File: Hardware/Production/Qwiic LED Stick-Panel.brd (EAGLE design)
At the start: 111.5 x 169.2 mm, 558 parts, among them J13 QWIIC_RA, J14 QWIIC_RA, J15 AVR_SPI_PROG_3X2TESTPOINTS, J19 QWIIC_RA, J2 QWIIC_RA, J20 QWIIC_RA, J21 AVR_SPI_PROG_3X2TESTPOINTS, J25 QWIIC_RA, J26 QWIIC_RA, J27 AVR_SPI_PROG_3X2TESTPOINTS, J3 QWIIC_RA, J31 QWIIC_RA, J32 QWIIC_RA, J33 AVR_SPI_PROG_3X2TESTPOINTS, J4 QWIIC_RA, J6 AVR_SPI_PROG_3X2TESTPOINTS, J8 QWIIC_RA, J9 AVR_SPI_PROG_3X2TESTPOINTS, U1 ATTINY85, U2 ATTINY85, U3 ATTINY85, U4 ATTINY85, U5 ATTINY85, U6 ATTINY85

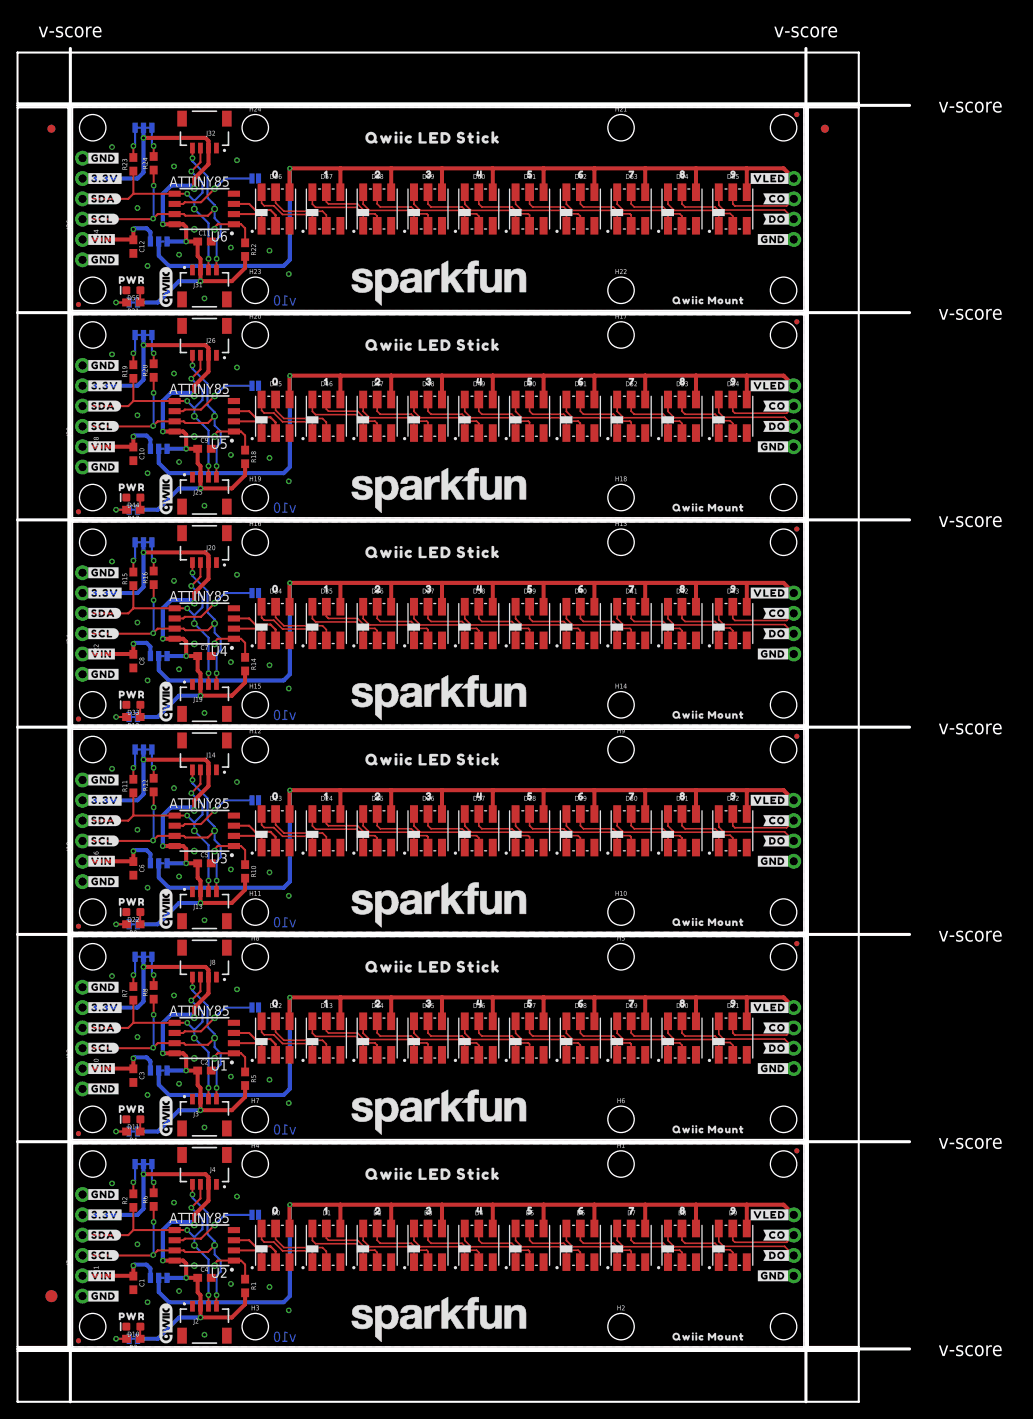
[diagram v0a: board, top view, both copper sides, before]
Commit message: Re-panelize
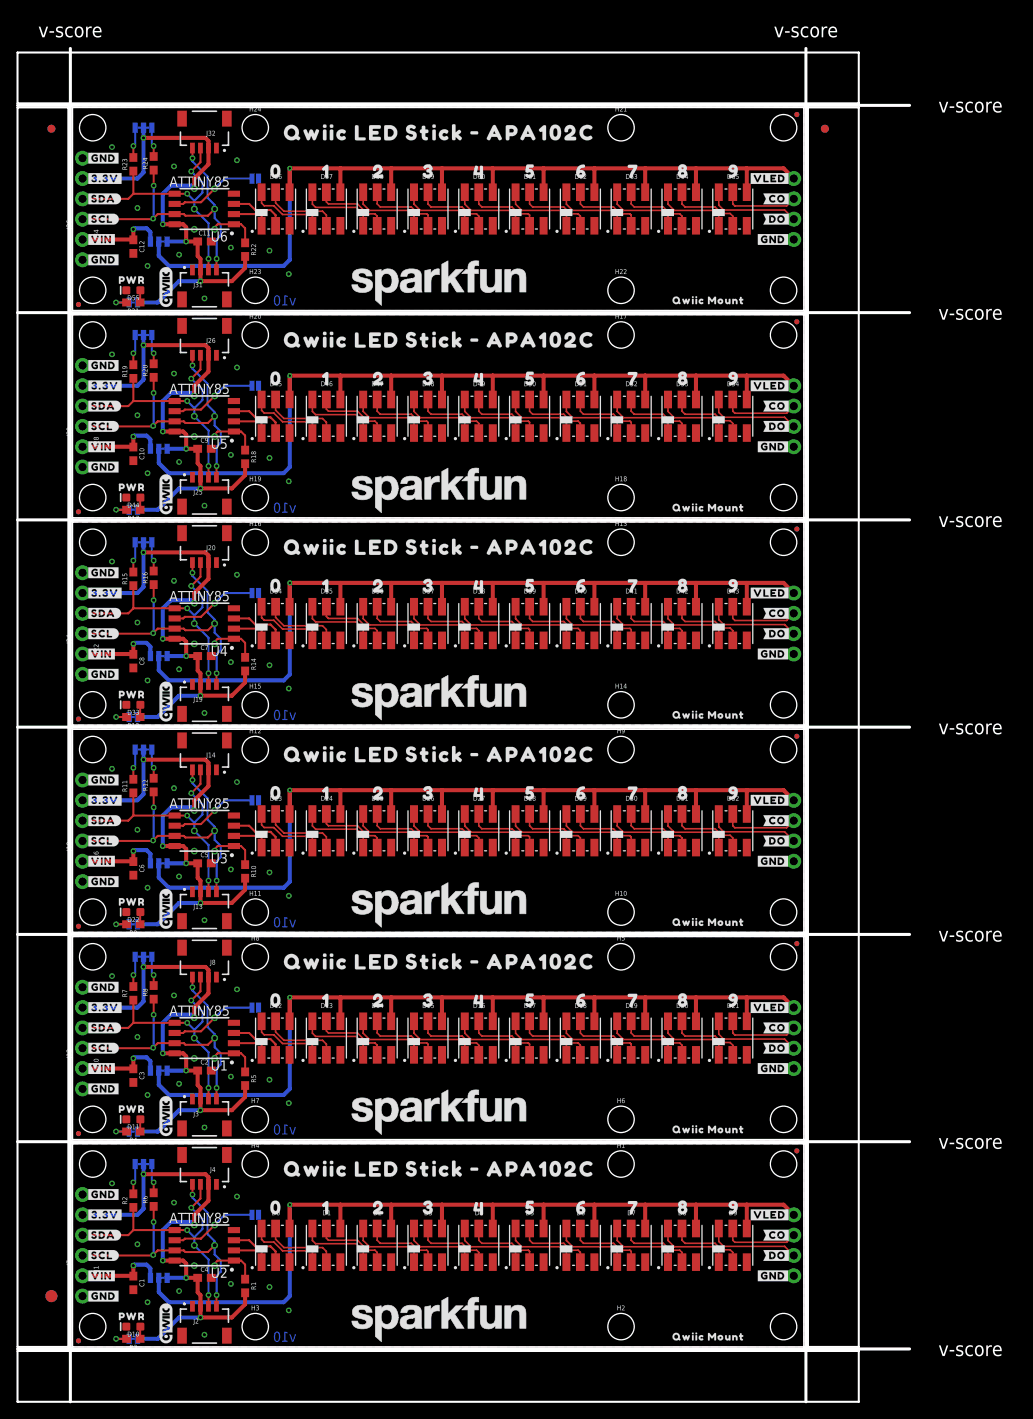
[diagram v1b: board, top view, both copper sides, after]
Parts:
- U$117, U$118, U$164, U$165, U$211, U$212, U$258, U$259, U$70, U$71: device output:QWIIC_LED_STICK0 -> output:#VIN#0
- U$119, U$166, U$213, U$260, U$72: device output:#VIN#0 -> output:VLED0
- U$120, U$167, U$214, U$261, U$73: device output:#VIN#0 -> output:#3#3V#1
- U$121, U$168, U$215, U$262, U$74: device output:VLED0 -> output:#VIN#4
- U$122, U$169, U$216, U$263, U$75: device output:#3#3V#1 -> output:QWIIC_MOUNT5
- U$123, U$170, U$217, U$264, U$76: device output:#VIN#4 -> output:00
- U$124, U$171, U$218, U$265, U$77: device output:QWIIC_MOUNT5 -> output:10
- U$125, U$172, U$219, U$266, U$78: device output:00 -> output:20
- U$126, U$173, U$220, U$267, U$79: device output:10 -> output:30
- U$127, U$174, U$221, U$268, U$80: device output:20 -> output:40
- U$128, U$175, U$222, U$269, U$81: device output:30 -> output:50
- U$129, U$176, U$223, U$270, U$82: device output:40 -> output:60
- U$13: device output:QWIIC_LED_STICK0 -> Labels-0_04:(I_SUPER2_C)
- U$130, U$177, U$224, U$271, U$83: device output:50 -> output:70
- U$131, U$178, U$225, U$272, U$84: device output:60 -> output:80
- U$132, U$179, U$226, U$273, U$85: device output:70 -> output:90
- U$133, U$180, U$227, U$274, U$86: device output:80 -> output:RED0
- U$134, U$181, U$228, U$275, U$87: device output:90 -> output:BLUE0
- U$135, U$182, U$229, U$276, U$88: device output:RED0 -> output:GREEN0
- U$136, U$183, U$230, U$277, U$89: device output:BLUE0 -> output:YELLOW0
- U$137, U$184, U$231, U$278, U$90: device output:GREEN0 -> output:OPEN#_0X230
- U$138, U$185, U$232, U$279, U$91: device output:YELLOW0 -> output:CLOSED#_0X220
- U$139, U$186, U$233, U$280, U$92: device output:OPEN#_0X230 -> output:QWIIC_MOUNT5
- U$140, U$187, U$234, U$281, U$93: device output:CLOSED#_0X220 -> output:QWIIC_LED_STICK_#_APA102C0
- U$141, U$188, U$235, U$282, U$94: device output:QWIIC_MOUNT5 -> output:QWIIC_LED_STICK_#_APA102C0
- U$27: device output:QWIIC_LED_STICK0 -> output:#GND#0
- U$48: device Labels-0_04:(I_SUPER2_C) -> output:QWIIC_LED_STICK_#_APA102C0
- U$49: device output:#GND#0 -> output:QWIIC_LED_STICK_#_APA102C0
- moved U$49 65.8 mm to (66.7, 22.2), flipped to the bottom
- moved U$122 57.7 mm to (74.3, 53.1), flipped to the top
- moved U$169 57.7 mm to (74.3, 79.0), flipped to the top
- moved U$216 57.7 mm to (74.3, 104.9), flipped to the top
- moved U$263 57.7 mm to (74.3, 130.8), flipped to the top
- moved U$75 57.7 mm to (74.3, 27.2), flipped to the top
- moved U$139 56.1 mm to (84.5, 53.1)
- moved U$186 56.1 mm to (84.5, 79.0)
- moved U$233 56.1 mm to (84.5, 104.9)
- moved U$280 56.1 mm to (84.5, 130.8)
- moved U$92 56.1 mm to (84.5, 27.2)
- moved U$27 53.9 mm to (1.65, 32.3), flipped to the top
- moved U$138 53.5 mm to (30.0, 64.8)
- moved U$185 53.5 mm to (30.0, 90.7)
- moved U$232 53.5 mm to (30.0, 116.6)
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- renumbered LED_PWR to VLED, LED_PWR1 to VLED1, LED_PWR2 to VLED2, LED_PWR3 to VLED3, LED_PWR4 to VLED4, LED_PWR5 to VLED5
